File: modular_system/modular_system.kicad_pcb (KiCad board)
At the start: 2 copper layers, 97.2 x 48.5 mm, 12 parts, among them J1 Screw_Terminal_01x02, J2 Conn_01x01_Male, J3 Conn_01x01_Male, J4 Conn_01x01_Male, J5 Conn_01x01_Male, J6 Conn_01x04_Female, J7 Conn_01x04_Female, U1 BluePill_STM32F103C

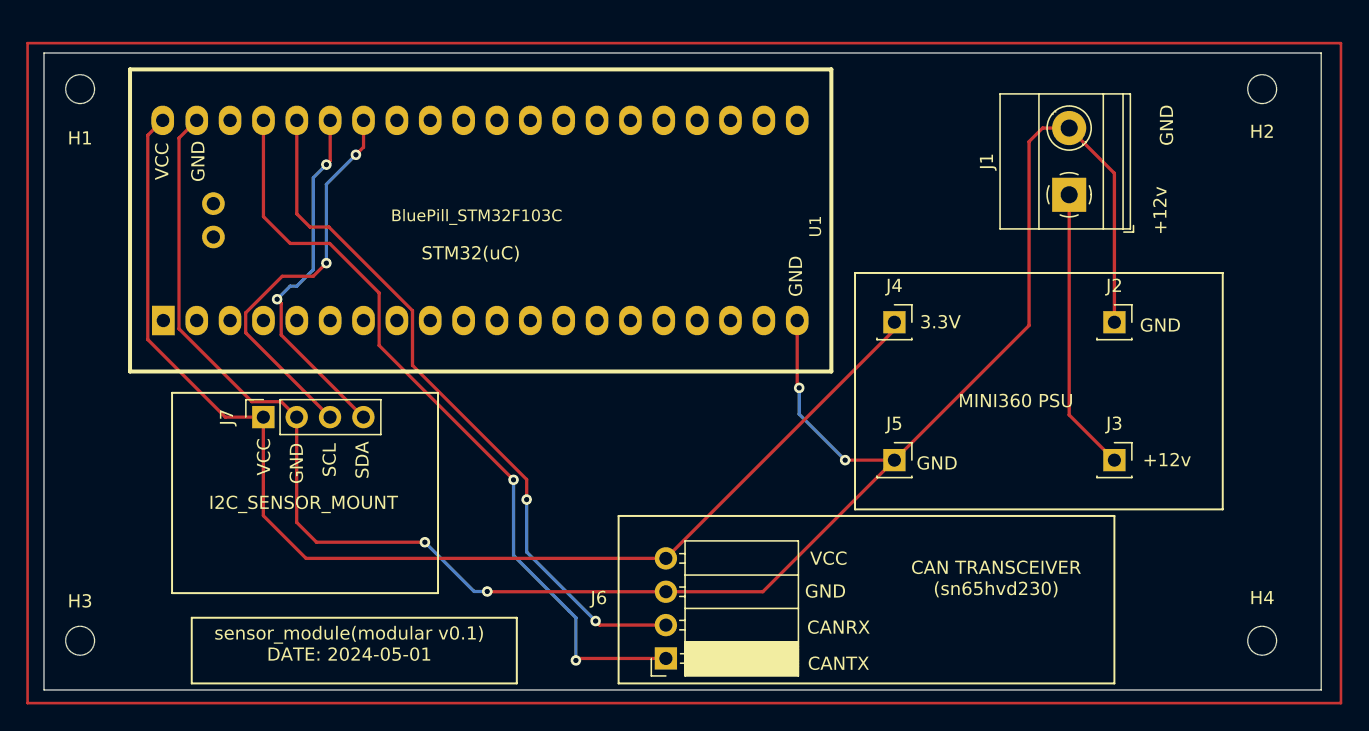
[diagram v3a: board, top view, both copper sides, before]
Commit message: updated to use ISO M3 sized mounting holes
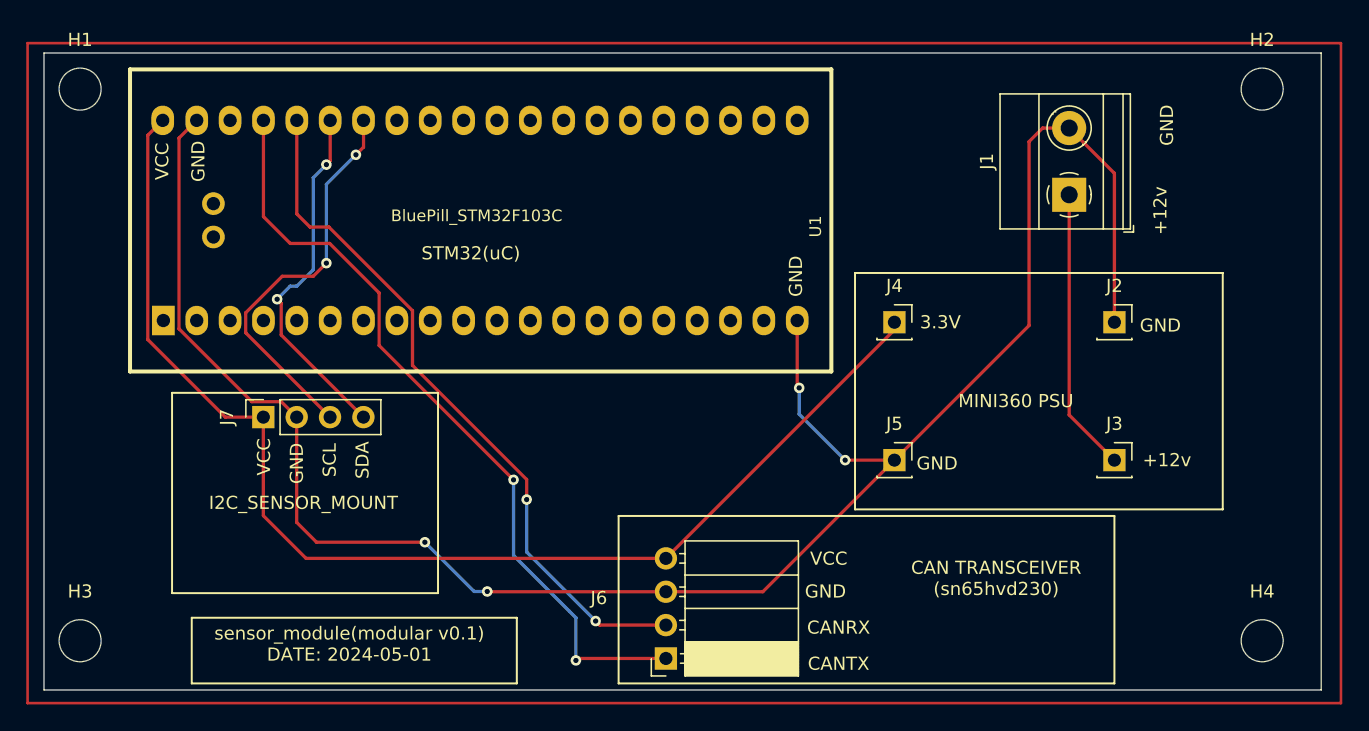
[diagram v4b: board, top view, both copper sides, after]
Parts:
- H1, H2, H3, H4: footprint MountingHole:MountingHole_2.2mm_M2_ISO14580 -> MountingHole:MountingHole_3.2mm_M3_ISO14580
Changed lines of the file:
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@@
     )
   )
-  (footprint "MountingHole:MountingHole_2.2mm_M2_ISO14580" locked (layer "F.Cu")
+  (footprint "MountingHole:MountingHole_3.2mm_M3_ISO14580" locked (layer "F.Cu")
     (at 193.75 95.25)
-    (descr "Mounting Hole 2.2mm, no annular, M2, ISO14580")
-    (tags "mounting hole 2.2mm no annular m2 iso14580")
+    (descr "Mounting Hole 3.2mm, no annular, M3, ISO14580")
+    (tags "mounting hole 3.2mm no annular m3 iso14580")
     (property "Sheetfile" "modular_system.kicad_sch")
     (property "Sheetname" "")
     (attr exclude_from_pos_files)
-    (fp_text reference "H4" (at 0 -3.25) (layer "F.SilkS")
-      (effects (font (size 1 1) (thickness 0.15)))
-    )
-    (fp_text value "MountingHole" (at 0 2.9) (layer "F.Fab")
-      (effects (font (size 1 1) (thickness 0.15)))
-    )
-    (fp_text user "${REFERENCE}" (at 0 0) (layer "F.Fab")
-      (effects (font (size 1 1) (thickness 0.15)))
-    )
-    (fp_circle (center 0 0) (end 1.9 0) (layer "Cmts.User") (width 0.15) (fill none))
-    (fp_circle (center 0 0) (end 2.15 0) (layer "F.CrtYd") (width 0.05) (fill none))
-    (pad "" np_thru_hole circle locked (at 0 0) (size 2.2 2.2) (drill 2.2) (layers *.Cu *.Mask))
+    (fp_text reference "H4" (at 0 -3.75) (layer "F.SilkS")
+      (effects (font (size 1 1) (thickness 0.15)))
+    )
+    (fp_text value "MountingHole" (at 0 3.75) (layer "F.Fab")
+      (effects (font (size 1 1) (thickness 0.15)))
+    )
+    (fp_text user "${REFERENCE}" (at 0 0) (layer "F.Fab")
+      (effects (font (size 1 1) (thickness 0.15)))
+    )
+    (fp_circle (center 0 0) (end 2.75 0) (layer "Cmts.User") (width 0.15) (fill none))
+    (fp_circle (center 0 0) (end 3 0) (layer "F.CrtYd") (width 0.05) (fill none))
+    (pad "" np_thru_hole circle locked (at 0 0) (size 3.2 3.2) (drill 3.2) (layers *.Cu *.Mask))
   )
   (footprint "BluePill_breakouts:BluePill_STM32F103C" locked (layer "F.Cu")
@@
     )
   )
-  (footprint "MountingHole:MountingHole_2.2mm_M2_ISO14580" locked (layer "F.Cu")
+  (footprint "MountingHole:MountingHole_3.2mm_M3_ISO14580" locked (layer "F.Cu")
     (at 193.75 53.25)
-    (descr "Mounting Hole 2.2mm, no annular, M2, ISO14580")
-    (tags "mounting hole 2.2mm no annular m2 iso14580")
+    (descr "Mounting Hole 3.2mm, no annular, M3, ISO14580")
+    (tags "mounting hole 3.2mm no annular m3 iso14580")
     (property "Sheetfile" "modular_system.kicad_sch")
     (property "Sheetname" "")
     (attr exclude_from_pos_files)
-    (fp_text reference "H2" (at 0 3.25) (layer "F.SilkS")
-      (effects (font (size 1 1) (thickness 0.15)))
-    )
-    (fp_text value "MountingHole" (at 0 2.9) (layer "F.Fab")
-      (effects (font (size 1 1) (thickness 0.15)))
-    )
-    (fp_text user "${REFERENCE}" (at 0 0) (layer "F.Fab")
-      (effects (font (size 1 1) (thickness 0.15)))
-    )
-    (fp_circle (center 0 0) (end 1.9 0) (layer "Cmts.User") (width 0.15) (fill none))
-    (fp_circle (center 0 0) (end 2.15 0) (layer "F.CrtYd") (width 0.05) (fill none))
-    (pad "" np_thru_hole circle locked (at 0 0) (size 2.2 2.2) (drill 2.2) (layers *.Cu *.Mask))
-  )
-  (footprint "MountingHole:MountingHole_2.2mm_M2_ISO14580" locked (layer "F.Cu")
+    (fp_text reference "H2" (at 0 -3.75) (layer "F.SilkS")
+      (effects (font (size 1 1) (thickness 0.15)))
+    )
+    (fp_text value "MountingHole" (at 0 3.75) (layer "F.Fab")
+      (effects (font (size 1 1) (thickness 0.15)))
+    )
+    (fp_text user "${REFERENCE}" (at 0 0) (layer "F.Fab")
+      (effects (font (size 1 1) (thickness 0.15)))
+    )
+    (fp_circle (center 0 0) (end 2.75 0) (layer "Cmts.User") (width 0.15) (fill none))
+    (fp_circle (center 0 0) (end 3 0) (layer "F.CrtYd") (width 0.05) (fill none))
+    (pad "" np_thru_hole circle locked (at 0 0) (size 3.2 3.2) (drill 3.2) (layers *.Cu *.Mask))
+  )
+  (footprint "MountingHole:MountingHole_3.2mm_M3_ISO14580" locked (layer "F.Cu")
     (at 103.75 95.25)
-    (descr "Mounting Hole 2.2mm, no annular, M2, ISO14580")
-    (tags "mounting hole 2.2mm no annular m2 iso14580")
+    (descr "Mounting Hole 3.2mm, no annular, M3, ISO14580")
+    (tags "mounting hole 3.2mm no annular m3 iso14580")
     (property "Sheetfile" "modular_system.kicad_sch")
     (property "Sheetname" "")
     (attr exclude_from_pos_files)
-    (fp_text reference "H3" (at 0 -3) (layer "F.SilkS")
-      (effects (font (size 1 1) (thickness 0.15)))
-    )
-    (fp_text value "MountingHole" (at 0 2.9) (layer "F.Fab")
-      (effects (font (size 1 1) (thickness 0.15)))
-    )
-    (fp_text user "${REFERENCE}" (at 0 0) (layer "F.Fab")
-      (effects (font (size 1 1) (thickness 0.15)))
-    )
-    (fp_circle (center 0 0) (end 1.9 0) (layer "Cmts.User") (width 0.15) (fill none))
-    (fp_circle (center 0 0) (end 2.15 0) (layer "F.CrtYd") (width 0.05) (fill none))
-    (pad "" np_thru_hole circle locked (at 0 0) (size 2.2 2.2) (drill 2.2) (layers *.Cu *.Mask))
+    (fp_text reference "H3" (at 0 -3.75) (layer "F.SilkS")
+      (effects (font (size 1 1) (thickness 0.15)))
+    )
+    (fp_text value "MountingHole" (at 0 3.75) (layer "F.Fab")
+      (effects (font (size 1 1) (thickness 0.15)))
+    )
+    (fp_text user "${REFERENCE}" (at 0 0) (layer "F.Fab")
+      (effects (font (size 1 1) (thickness 0.15)))
+    )
+    (fp_circle (center 0 0) (end 2.75 0) (layer "Cmts.User") (width 0.15) (fill none))
+    (fp_circle (center 0 0) (end 3 0) (layer "F.CrtYd") (width 0.05) (fill none))
+    (pad "" np_thru_hole circle locked (at 0 0) (size 3.2 3.2) (drill 3.2) (layers *.Cu *.Mask))
   )
   (footprint "Connector_PinSocket_2.54mm:PinSocket_1x01_P2.54mm_Vertical" locked (layer "F.Cu")
@@
     )
   )
-  (footprint "MountingHole:MountingHole_2.2mm_M2_ISO14580" locked (layer "F.Cu")
+  (footprint "MountingHole:MountingHole_3.2mm_M3_ISO14580" locked (layer "F.Cu")
     (at 103.75 53.25)
-    (descr "Mounting Hole 2.2mm, no annular, M2, ISO14580")
-    (tags "mounting hole 2.2mm no annular m2 iso14580")
+    (descr "Mounting Hole 3.2mm, no annular, M3, ISO14580")
+    (tags "mounting hole 3.2mm no annular m3 iso14580")
     (property "Sheetfile" "modular_system.kicad_sch")
     (property "Sheetname" "")
     (attr exclude_from_pos_files)
-    (fp_text reference "H1" (at 0 3.75) (layer "F.SilkS")
-      (effects (font (size 1 1) (thickness 0.15)))
-    )
-    (fp_text value "MountingHole" (at 0 2.9) (layer "F.Fab")
-      (effects (font (size 1 1) (thickness 0.15)))
-    )
-    (fp_text user "${REFERENCE}" (at 0 0) (layer "F.Fab")
-      (effects (font (size 1 1) (thickness 0.15)))
-    )
-    (fp_circle (center 0 0) (end 1.9 0) (layer "Cmts.User") (width 0.15) (fill none))
-    (fp_circle (center 0 0) (end 2.15 0) (layer "F.CrtYd") (width 0.05) (fill none))
-    (pad "" np_thru_hole circle locked (at 0 0) (size 2.2 2.2) (drill 2.2) (layers *.Cu *.Mask))
+    (fp_text reference "H1" (at 0 -3.75) (layer "F.SilkS")
+      (effects (font (size 1 1) (thickness 0.15)))
+    )
+    (fp_text value "MountingHole" (at 0 3.75) (layer "F.Fab")
+      (effects (font (size 1 1) (thickness 0.15)))
+    )
+    (fp_text user "${REFERENCE}" (at 0 0) (layer "F.Fab")
+      (effects (font (size 1 1) (thickness 0.15)))
+    )
+    (fp_circle (center 0 0) (end 2.75 0) (layer "Cmts.User") (width 0.15) (fill none))
+    (fp_circle (center 0 0) (end 3 0) (layer "F.CrtYd") (width 0.05) (fill none))
+    (pad "" np_thru_hole circle locked (at 0 0) (size 3.2 3.2) (drill 3.2) (layers *.Cu *.Mask))
   )
   (footprint "TerminalBlock_Phoenix:TerminalBlock_Phoenix_MKDS-1,5-2-5.08_1x02_P5.08mm_Horizontal" (layer "F.Cu")

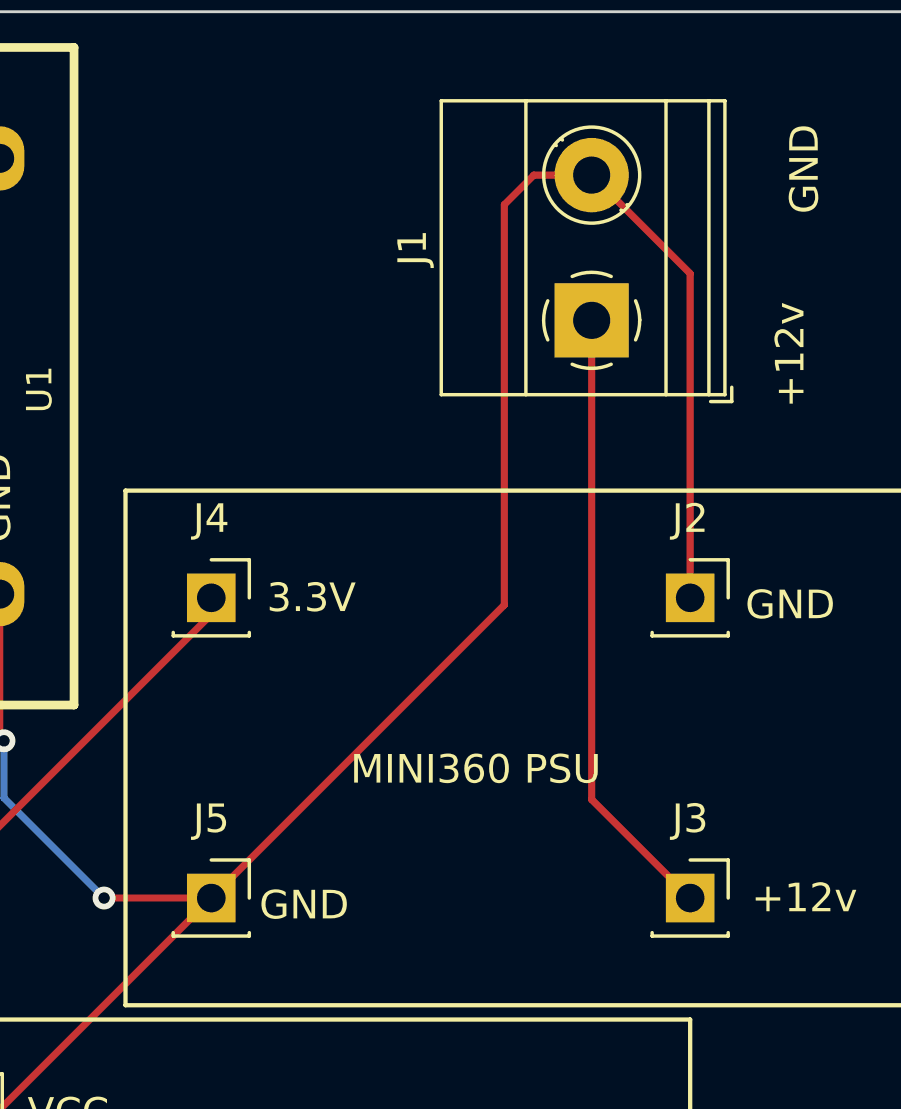
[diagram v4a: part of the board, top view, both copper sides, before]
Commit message: Fixed the mini360 pin spacing and placement. Swapped the J3 & J4 pins.
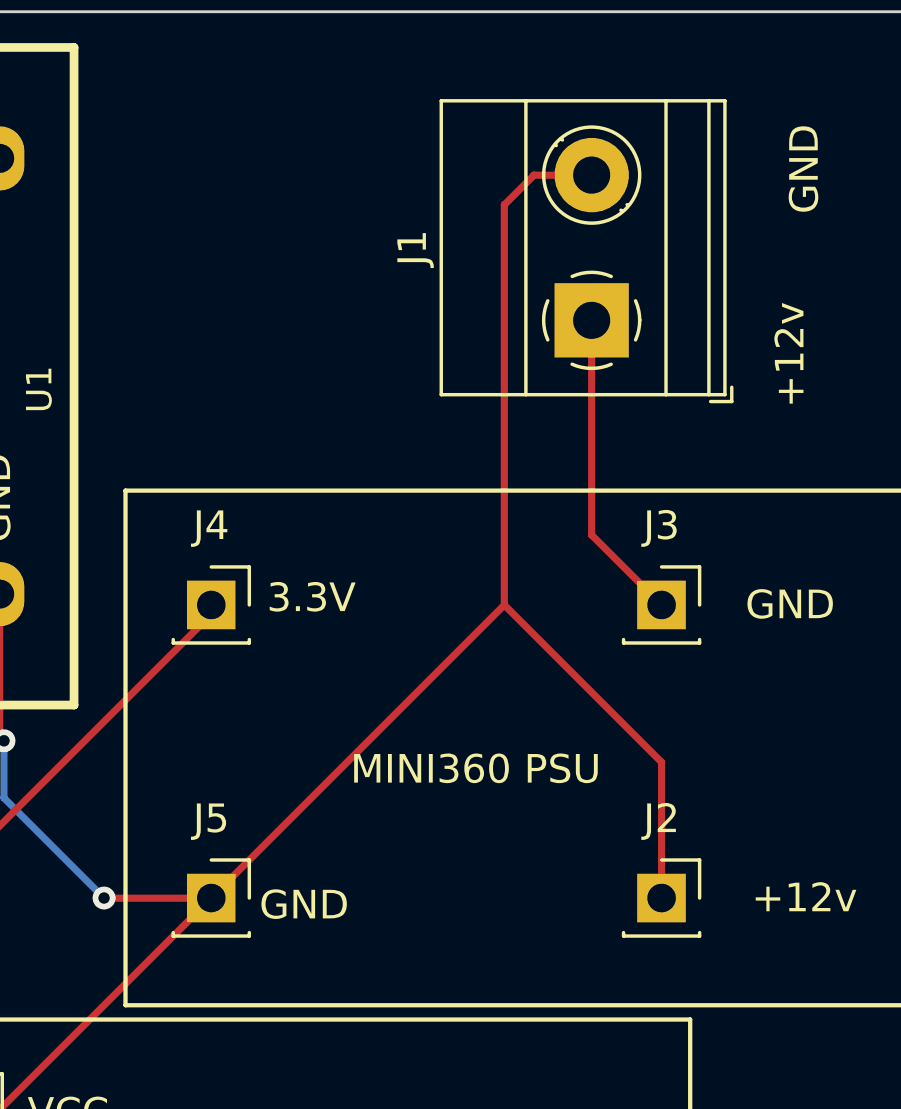
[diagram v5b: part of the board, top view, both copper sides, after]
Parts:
- moved J2 10.5 mm to (181.5, 81.5)
- moved J3 10.3 mm to (181.5, 71.2)
- moved J4 0.25 mm to (165.8, 71.2)
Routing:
- net Net-(J1-Pad1): track 21.6 -> 11.0 mm
- net GND: track 152.1 -> 148.4 mm
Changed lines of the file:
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@@
     )
   )
-  (footprint "Connector_PinSocket_2.54mm:PinSocket_1x01_P2.54mm_Vertical" locked (layer "F.Cu")
-    (at 182.5 81.5)
+  (footprint "Connector_PinSocket_2.54mm:PinSocket_1x01_P2.54mm_Vertical" (layer "F.Cu")
+    (at 181.5 71.25)
     (descr "Through hole straight socket strip, 1x01, 2.54mm pitch, single row (from Kicad 4.0.7), script generated")
     (tags "Through hole socket strip THT 1x01 2.54mm single row")
@@
     (fp_line (start 0.635 -1.27) (end 1.27 -0.635) (layer "F.Fab") (width 0.1))
     (fp_line (start 1.27 -0.635) (end 1.27 1.27) (layer "F.Fab") (width 0.1))
-    (pad "1" thru_hole rect locked (at 0 0) (size 1.7 1.7) (drill 1) (layers *.Cu *.Mask)
+    (pad "1" thru_hole rect (at 0 0) (size 1.7 1.7) (drill 1) (layers *.Cu *.Mask)
       (net 1 "Net-(J1-Pad1)") (pinfunction "Pin_1") (pintype "passive"))
     (model "${KICAD6_3DMODEL_DIR}/Connector_PinSocket_2.54mm.3dshapes/PinSocket_1x01_P2.54mm_Vertical.wrl"
@@
     )
   )
-  (footprint "Connector_PinSocket_2.54mm:PinSocket_1x01_P2.54mm_Vertical" locked (layer "F.Cu")
-    (at 165.75 71)
+  (footprint "Connector_PinSocket_2.54mm:PinSocket_1x01_P2.54mm_Vertical" (layer "F.Cu")
+    (at 165.75 71.25)
     (descr "Through hole straight socket strip, 1x01, 2.54mm pitch, single row (from Kicad 4.0.7), script generated")
     (tags "Through hole socket strip THT 1x01 2.54mm single row")
@@
     (fp_line (start 0.635 -1.27) (end 1.27 -0.635) (layer "F.Fab") (width 0.1))
     (fp_line (start 1.27 1.27) (end -1.27 1.27) (layer "F.Fab") (width 0.1))
-    (pad "1" thru_hole rect locked (at 0 0) (size 1.7 1.7) (drill 1) (layers *.Cu *.Mask)
+    (pad "1" thru_hole rect (at 0 0) (size 1.7 1.7) (drill 1) (layers *.Cu *.Mask)
       (net 2 "/Vcc") (pinfunction "Pin_1") (pintype "passive"))
     (model "${KICAD6_3DMODEL_DIR}/Connector_PinSocket_2.54mm.3dshapes/PinSocket_1x01_P2.54mm_Vertical.wrl"
@@
     (pad "" np_thru_hole circle locked (at 0 0) (size 3.2 3.2) (drill 3.2) (layers *.Cu *.Mask))
   )
-  (footprint "Connector_PinSocket_2.54mm:PinSocket_1x01_P2.54mm_Vertical" locked (layer "F.Cu")
-    (at 182.5 71)
+  (footprint "Connector_PinSocket_2.54mm:PinSocket_1x01_P2.54mm_Vertical" (layer "F.Cu")
+    (at 181.5 81.5)
     (descr "Through hole straight socket strip, 1x01, 2.54mm pitch, single row (from Kicad 4.0.7), script generated")
     (tags "Through hole socket strip THT 1x01 2.54mm single row")
@@
     (style (thickness 0.15) (arrow_length 1.27) (text_position_mode 0) (extension_height 0.58642) (extension_offset 0.5) keep_text_aligned)
   )
-  (segment (start 179.055 78.055) (end 179.055 61.295) (width 0.25) (layer "F.Cu") (net 1))
-  (segment (start 182.5 81.5) (end 179.055 78.055) (width 0.25) (layer "F.Cu") (net 1))
+  (segment (start 179.055 68.805) (end 181.5 71.25) (width 0.25) (layer "F.Cu") (net 1))
+  (segment (start 179.055 61.295) (end 179.055 68.805) (width 0.25) (layer "F.Cu") (net 1))
   (segment (start 117.7 78.225) (end 114.806578 78.225) (width 0.25) (layer "F.Cu") (net 2))
   (segment (start 108.901089 72.319511) (end 108.901089 56.767311) (width 0.25) (layer "F.Cu") (net 2))
@@
   (segment (start 114.806578 78.225) (end 108.901089 72.319511) (width 0.25) (layer "F.Cu") (net 2))
   (segment (start 117.7 85.725) (end 120.955 88.98) (width 0.25) (layer "F.Cu") (net 2))
+  (segment (start 181.5 76.75) (end 181.5 81.5) (width 0.25) (layer "F.Cu") (net 3))
   (segment (start 116.8278 77.050489) (end 111.277311 71.5) (width 0.25) (layer "F.Cu") (net 3))
   (segment (start 134.77 91.52) (end 134.75 91.5) (width 0.25) (layer "F.Cu") (net 3))
@@
   (segment (start 148.35 91.52) (end 134.77 91.52) (width 0.25) (layer "F.Cu") (net 3))
   (segment (start 120.24 78.225) (end 119.065489 77.050489) (width 0.25) (layer "F.Cu") (net 3))
-  (segment (start 182.5 71) (end 182.5 59.66) (width 0.25) (layer "F.Cu") (net 3))
   (segment (start 155.73 91.52) (end 165.75 81.5) (width 0.25) (layer "F.Cu") (net 3))
   (segment (start 176 57.25) (end 177.035 56.215) (width 0.25) (layer "F.Cu") (net 3))
@@
   (segment (start 130 87.75) (end 121.75 87.75) (width 0.25) (layer "F.Cu") (net 3))
   (segment (start 120.24 86.24) (end 120.24 78.225) (width 0.25) (layer "F.Cu") (net 3))
-  (segment (start 182.5 59.66) (end 179.055 56.215) (width 0.25) (layer "F.Cu") (net 3))
   (segment (start 165.75 81.5) (end 176 71.25) (width 0.25) (layer "F.Cu") (net 3))
   (segment (start 148.35 91.52) (end 155.73 91.52) (width 0.25) (layer "F.Cu") (net 3))
+  (segment (start 176 71.25) (end 181.5 76.75) (width 0.25) (layer "F.Cu") (net 3))
   (segment (start 111.277311 71.5) (end 111.277311 56.981889) (width 0.25) (layer "F.Cu") (net 3))
   (segment (start 177.035 56.215) (end 179.055 56.215) (width 0.25) (layer "F.Cu") (net 3))
